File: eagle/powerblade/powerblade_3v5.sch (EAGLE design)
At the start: 77 parts, among them J1 JTAG_14PIN_IDC-ND, J2 AC_INFINAL, J4 TC2030-JLINK-NL, Q1 NTS4173, Q4 2SK1829, U1 TPS62122, U2 MCP6V3, U3 MSP430FR5738, U4 NRF51822QF, U6 MAX9910, U7 OPA2369, X1 16MHz, X3 32.768kHz, Y1 UREACH_XTEND

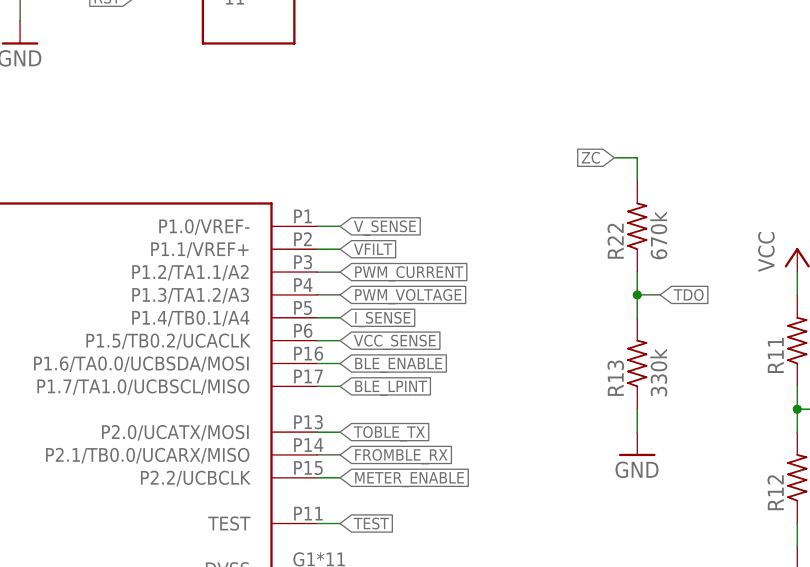
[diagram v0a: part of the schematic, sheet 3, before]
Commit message: cleaned up after removing header
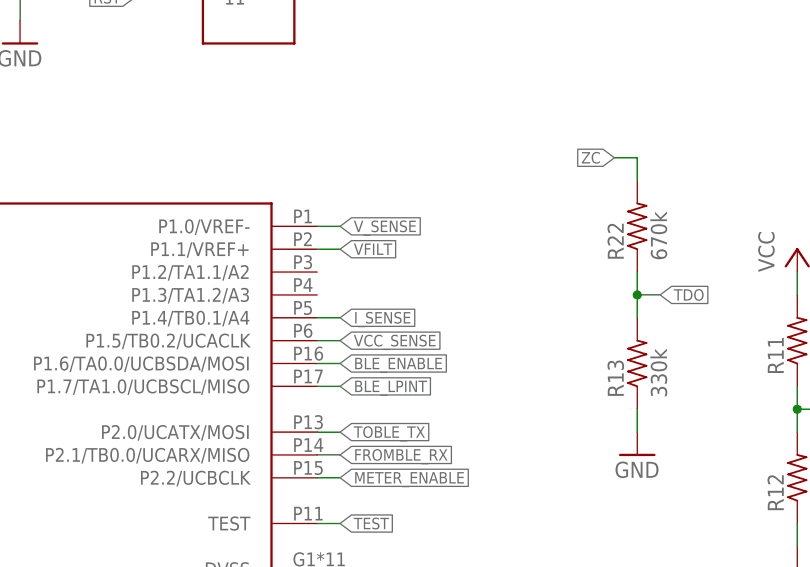
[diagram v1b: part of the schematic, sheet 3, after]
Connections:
- removed net PWM_CURRENT: U3.P1.2/TA1.1/A2
- removed net PWM_VOLTAGE: U3.P1.3/TA1.2/A3
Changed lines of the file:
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@@
-</segment>
-</net>
-<net name="PWM_CURRENT" class="0">
-<segment>
-<pinref part="U3" gate="G$1" pin="P1.2/TA1.1/A2"/>
-<wire x1="27.94" y1="12.7" x2="25.4" y2="12.7" width="0.1524" layer="91"/>
-<label x="27.94" y="12.7" size="1.27" layer="95" xref="yes"/>
-</segment>
-</net>
-<net name="PWM_VOLTAGE" class="0">
-<segment>
-<pinref part="U3" gate="G$1" pin="P1.3/TA1.2/A3"/>
-<wire x1="27.94" y1="10.16" x2="25.4" y2="10.16" width="0.1524" layer="91"/>
-<label x="27.94" y="10.16" size="1.27" layer="95" xref="yes"/>
 </segment>
 </net>
